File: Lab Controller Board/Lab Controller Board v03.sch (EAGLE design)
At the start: 36 parts, among them Q2 NPN - 2N5088, Q3 MOSFET-NCHANNELFQP30N06L, Q4 NPN - 2N5088, Q5 MOSFET-NCHANNELFQP30N06L, Q6 NPN - 2N5088, Q7 MOSFET-NCHANNELFQP30N06L, Q8 NPN - 2N5088, U1 ATMEGA328P_TQFP

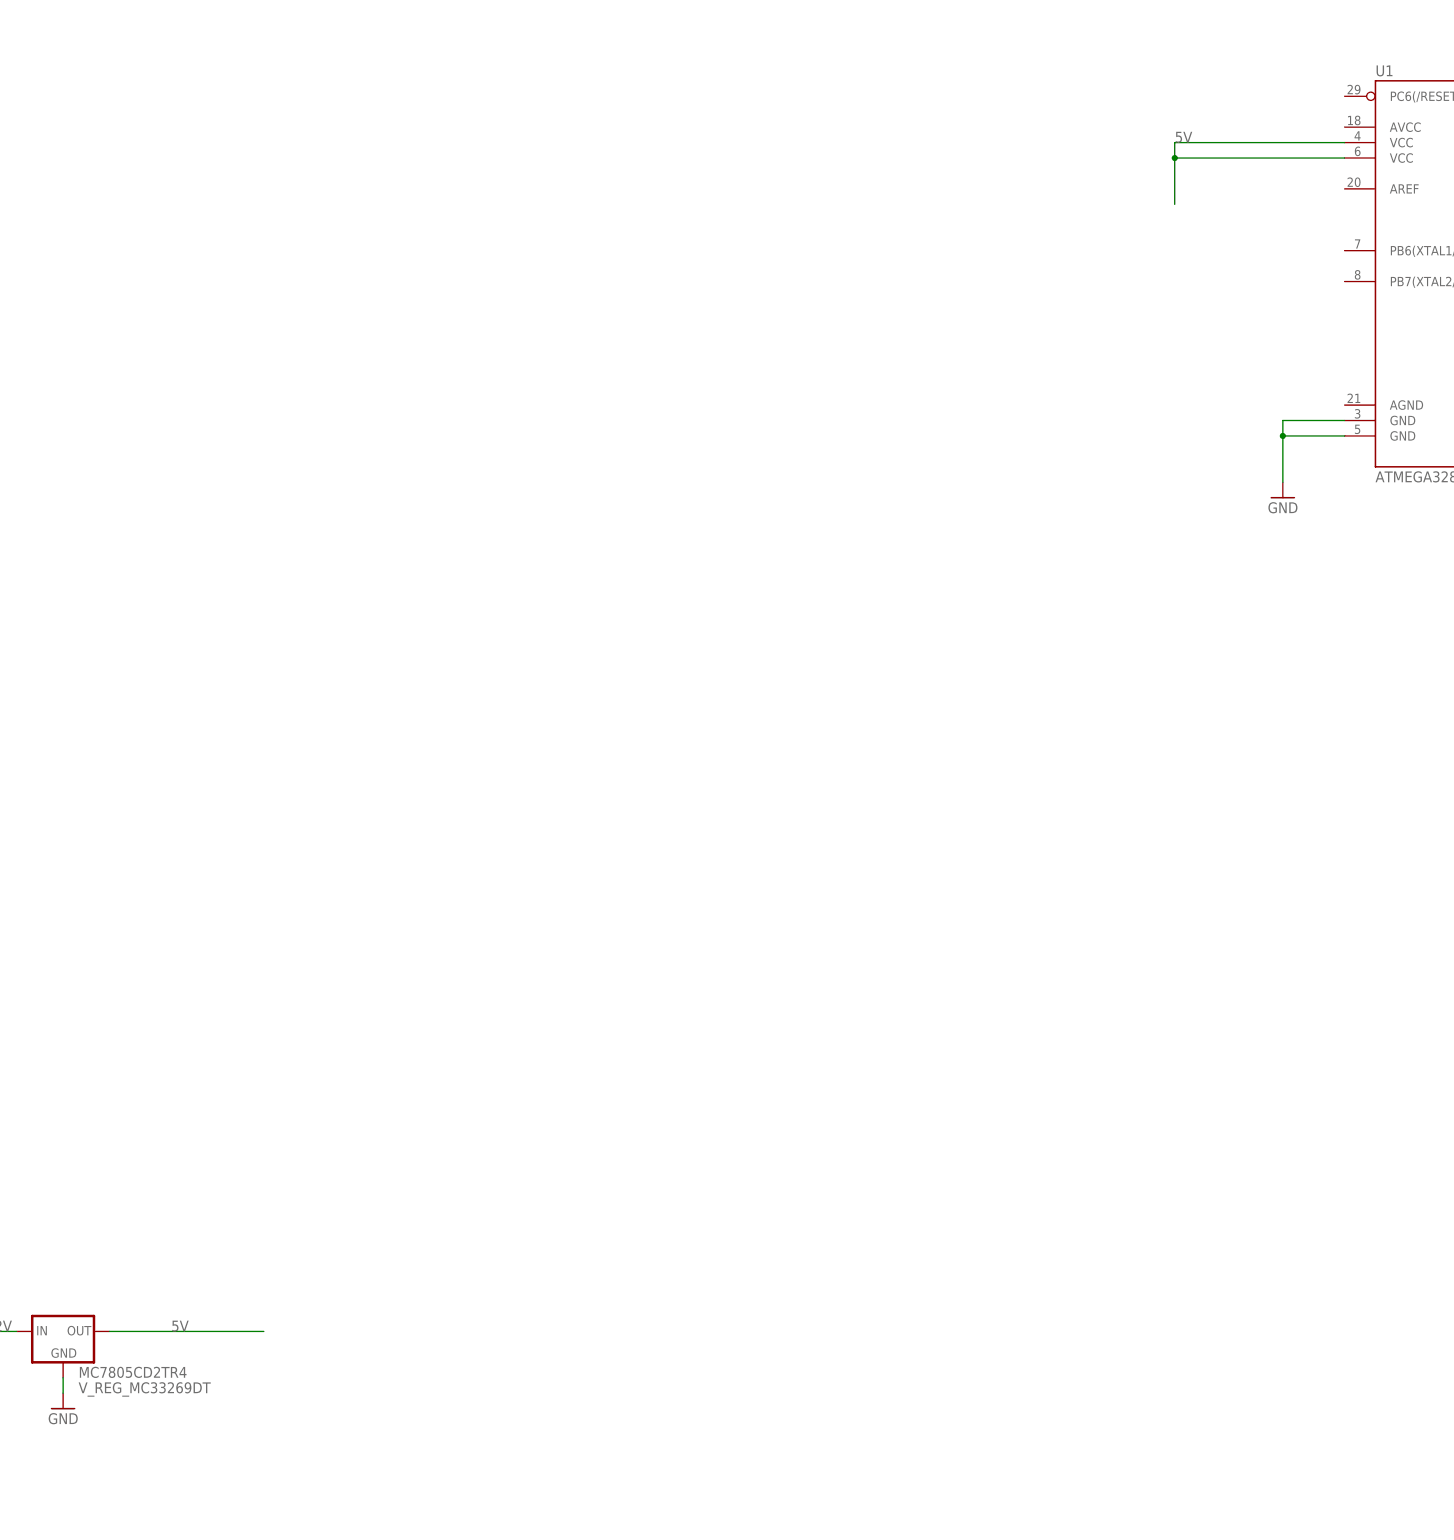
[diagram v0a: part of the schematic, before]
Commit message: SMD'ing the LAB Led Controller
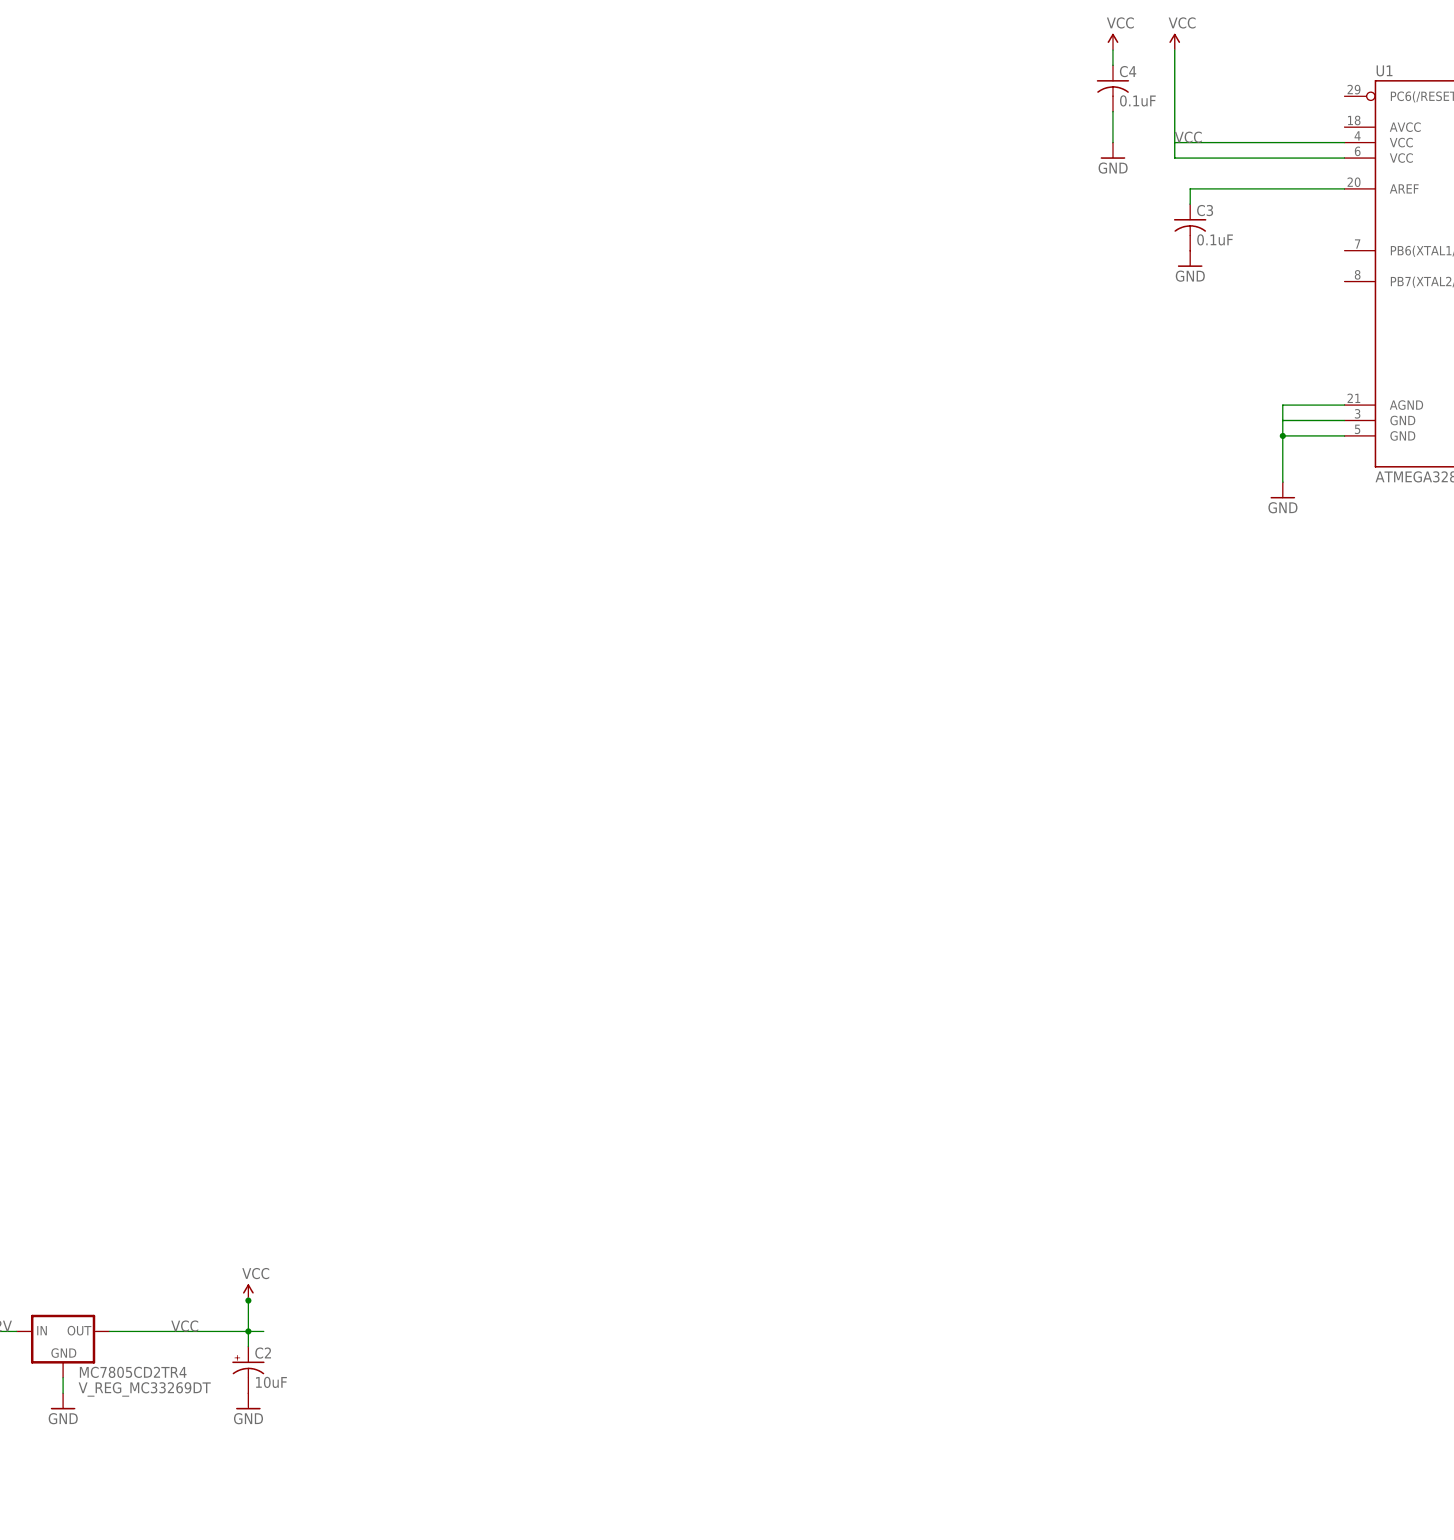
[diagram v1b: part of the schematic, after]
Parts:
- added C2: 10uF, SparkFun-Capacitors:CAP_POL3528
- added C3, C4: 0.1uF, resistor:C-USC0402
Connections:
- new net N$1: C3.1, U1.AREF
- new net VCC: C2.+, C4.1, MC7805CD2TR4.OUT, U1.VCC@4, U1.VCC@6
- net 5V: no longer MC7805CD2TR4.OUT, U1.VCC@4, U1.VCC@6
- net GND: now also C2.-, C3.2, C4.2, U1.AGND
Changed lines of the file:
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@@
 <?xml version="1.0" encoding="utf-8"?>
 <!DOCTYPE eagle SYSTEM "eagle.dtd">
-<eagle version="7.3.0">
+<eagle version="7.5.0">
 <drawing>
 <settings>
@@
 <layer number="113" name="IDFDebug" color="7" fill="1" visible="yes" active="yes"/>
 <layer number="114" name="Badge_Outline" color="11" fill="1" visible="no" active="no"/>
+<layer number="115" name="ReferenceISLANDS" color="7" fill="1" visible="yes" active="yes"/>
 <layer number="116" name="Patch_BOT" color="9" fill="4" visible="yes" active="yes"/>
 <layer number="118" name="Rect_Pads" color="7" fill="1" visible="yes" active="yes"/>
@@
 <part name="U1" library="SparkFun-DigitalIC" deviceset="ATMEGA328P_TQFP" device="" value="ATMEGA328P_TQFP"/>
 <part name="GND9" library="SparkFun-Aesthetics" deviceset="GND" device=""/>
+<part name="C2" library="SparkFun-Capacitors" deviceset="CAP_POL" device="3528" value="10uF"/>
+<part name="GND10" library="SparkFun-Aesthetics" deviceset="GND" device=""/>
+<part name="SUPPLY1" library="SparkFun-Aesthetics" deviceset="VCC" device=""/>
+<part name="SUPPLY2" library="SparkFun-Aesthetics" deviceset="VCC" device=""/>
+<part name="C3" library="resistor" deviceset="C-US" device="C0402" value="0.1uF"/>
+<part name="GND11" library="SparkFun-Aesthetics" deviceset="GND" device=""/>
+<part name="SUPPLY3" library="SparkFun-Aesthetics" deviceset="VCC" device=""/>
+<part name="C4" library="resistor" deviceset="C-US" device="C0402" value="0.1uF"/>
+<part name="GND12" library="SparkFun-Aesthetics" deviceset="GND" device=""/>
 </parts>
 <sheets>
@@
 <instance part="U1" gate="U$1" x="114.3" y="320.04"/>
 <instance part="GND9" gate="1" x="78.74" y="284.48" rot="MR0"/>
+<instance part="C2" gate="G$1" x="-91.44" y="142.24"/>
+<instance part="GND10" gate="1" x="-91.44" y="134.62" rot="MR0"/>
+<instance part="SUPPLY1" gate="G$1" x="60.96" y="358.14"/>
+<instance part="SUPPLY2" gate="G$1" x="-91.44" y="152.4"/>
+<instance part="C3" gate="G$1" x="63.5" y="330.2"/>
+<instance part="GND11" gate="1" x="63.5" y="322.58" rot="MR0"/>
+<instance part="SUPPLY3" gate="G$1" x="50.8" y="358.14"/>
+<instance part="C4" gate="G$1" x="50.8" y="353.06"/>
+<instance part="GND12" gate="1" x="50.8" y="340.36" rot="MR0"/>
 </instances>
 <busses>
@@
 <junction x="78.74" y="294.64"/>
 <pinref part="GND9" gate="1" pin="GND"/>
+<pinref part="U1" gate="U$1" pin="AGND"/>
+<wire x1="88.9" y1="299.72" x2="78.74" y2="299.72" width="0.1524" layer="91"/>
+<wire x1="78.74" y1="299.72" x2="78.74" y2="297.18" width="0.1524" layer="91"/>
+</segment>
+<segment>
+<pinref part="C2" gate="G$1" pin="-"/>
+<pinref part="GND10" gate="1" pin="GND"/>
+</segment>
+<segment>
+<pinref part="C3" gate="G$1" pin="2"/>
+<pinref part="GND11" gate="1" pin="GND"/>
+</segment>
+<segment>
+<pinref part="C4" gate="G$1" pin="2"/>
+<pinref part="GND12" gate="1" pin="GND"/>
+<wire x1="50.8" y1="342.9" x2="50.8" y2="347.98" width="0.1524" layer="91"/>
 </segment>
 </net>
@@
 <label x="88.9" y="2.54" size="1.778" layer="95"/>
 </segment>
-<segment>
-<pinref part="MC7805CD2TR4" gate="G$1" pin="OUT"/>
-<wire x1="-114.3" y1="147.32" x2="-88.9" y2="147.32" width="0.1524" layer="91"/>
-<label x="-104.14" y="147.32" size="1.778" layer="95"/>
-</segment>
+</net>
+<net name="N$6" class="0">
+<segment>
+<pinref part="LED1" gate="D1" pin="BLU-C"/>
+<pinref part="R11" gate="G$1" pin="2"/>
+</segment>
+</net>
+<net name="N$8" class="0">
+<segment>
+<pinref part="R12" gate="G$1" pin="2"/>
+<pinref part="LED1" gate="D1" pin="GRN-C"/>
+<wire x1="63.5" y1="-22.86" x2="71.12" y2="-22.86" width="0.1524" layer="91"/>
+</segment>
+</net>
+<net name="N$9" class="0">
+<segment>
+<pinref part="R13" gate="G$1" pin="2"/>
+<pinref part="LED1" gate="D1" pin="RED-C"/>
+<wire x1="55.88" y1="-25.4" x2="71.12" y2="-25.4" width="0.1524" layer="91"/>
+</segment>
+</net>
+<net name="9" class="0">
+<segment>
+<pinref part="JP6" gate="G$1" pin="2"/>
+<wire x1="119.38" y1="48.26" x2="58.42" y2="48.26" width="0.1524" layer="91"/>
+<label x="86.36" y="48.26" size="1.778" layer="95"/>
+</segment>
+</net>
+<net name="TX" class="0">
+<segment>
+<pinref part="JP6" gate="G$1" pin="12"/>
+<wire x1="119.38" y1="73.66" x2="58.42" y2="73.66" width="0.1524" layer="91"/>
+<label x="86.36" y="73.66" size="1.778" layer="95"/>
+</segment>
+</net>
+<net name="VCC" class="0">
 <segment>
 <pinref part="U1" gate="U$1" pin="VCC@4"/>
@@
 <wire x1="60.96" y1="342.9" x2="60.96" y2="340.36" width="0.1524" layer="91"/>
 <pinref part="U1" gate="U$1" pin="VCC@6"/>
-<wire x1="60.96" y1="340.36" x2="60.96" y2="332.74" width="0.1524" layer="91"/>
 <wire x1="88.9" y1="340.36" x2="60.96" y2="340.36" width="0.1524" layer="91"/>
-<junction x="60.96" y="340.36"/>
 <label x="60.96" y="342.9" size="1.778" layer="95"/>
-</segment>
-</net>
-<net name="N$6" class="0">
-<segment>
-<pinref part="LED1" gate="D1" pin="BLU-C"/>
-<pinref part="R11" gate="G$1" pin="2"/>
-</segment>
-</net>
-<net name="N$8" class="0">
-<segment>
-<pinref part="R12" gate="G$1" pin="2"/>
-<pinref part="LED1" gate="D1" pin="GRN-C"/>
-<wire x1="63.5" y1="-22.86" x2="71.12" y2="-22.86" width="0.1524" layer="91"/>
-</segment>
-</net>
-<net name="N$9" class="0">
-<segment>
-<pinref part="R13" gate="G$1" pin="2"/>
-<pinref part="LED1" gate="D1" pin="RED-C"/>
-<wire x1="55.88" y1="-25.4" x2="71.12" y2="-25.4" width="0.1524" layer="91"/>
-</segment>
-</net>
-<net name="9" class="0">
-<segment>
-<pinref part="JP6" gate="G$1" pin="2"/>
-<wire x1="119.38" y1="48.26" x2="58.42" y2="48.26" width="0.1524" layer="91"/>
-<label x="86.36" y="48.26" size="1.778" layer="95"/>
-</segment>
-</net>
-<net name="TX" class="0">
-<segment>
-<pinref part="JP6" gate="G$1" pin="12"/>
-<wire x1="119.38" y1="73.66" x2="58.42" y2="73.66" width="0.1524" layer="91"/>
-<label x="86.36" y="73.66" size="1.778" layer="95"/>
-</segment>
-</net>
+<pinref part="SUPPLY1" gate="G$1" pin="VCC"/>
+<wire x1="60.96" y1="342.9" x2="60.96" y2="358.14" width="0.1524" layer="91"/>
+</segment>
+<segment>
+<pinref part="MC7805CD2TR4" gate="G$1" pin="OUT"/>
+<wire x1="-114.3" y1="147.32" x2="-91.44" y2="147.32" width="0.1524" layer="91"/>
+<label x="-104.14" y="147.32" size="1.778" layer="95"/>
+<pinref part="C2" gate="G$1" pin="+"/>
+<wire x1="-91.44" y1="147.32" x2="-88.9" y2="147.32" width="0.1524" layer="91"/>
+<wire x1="-91.44" y1="147.32" x2="-91.44" y2="144.78" width="0.1524" layer="91"/>
+<junction x="-91.44" y="147.32"/>
+<pinref part="SUPPLY2" gate="G$1" pin="VCC"/>
+<wire x1="-91.44" y1="147.32" x2="-91.44" y2="152.4" width="0.1524" layer="91"/>
+<junction x="-91.44" y="152.4"/>
+</segment>
+<segment>
+<pinref part="SUPPLY3" gate="G$1" pin="VCC"/>
+<pinref part="C4" gate="G$1" pin="1"/>
+<wire x1="50.8" y1="355.6" x2="50.8" y2="358.14" width="0.1524" layer="91"/>
+</segment>
+</net>
+<net name="N$1" class="0">
+<segment>
+<pinref part="U1" gate="U$1" pin="AREF"/>
+<wire x1="88.9" y1="335.28" x2="63.5" y2="335.28" width="0.1524" layer="91"/>
+<wire x1="63.5" y1="335.28" x2="63.5" y2="332.74" width="0.1524" layer="91"/>
+<pinref part="C3" gate="G$1" pin="1"/>
+</segment>
+</net>
